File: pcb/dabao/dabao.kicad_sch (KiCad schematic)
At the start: 83 parts, among them J1 USB_C_Receptacle_USB2.0_16P, J2 USB_C_Receptacle_USB2.0_16P, J3 Conn_01x04_Pin, J4 Conn_01x04_Pin, J5 Conn_Battery, J6 MJ-4PP-9, SW1 SW_RESET, SW2 SW_POWER, U1 nice_nano, U2 MCP23017_SP, U3 MCP23017_SO

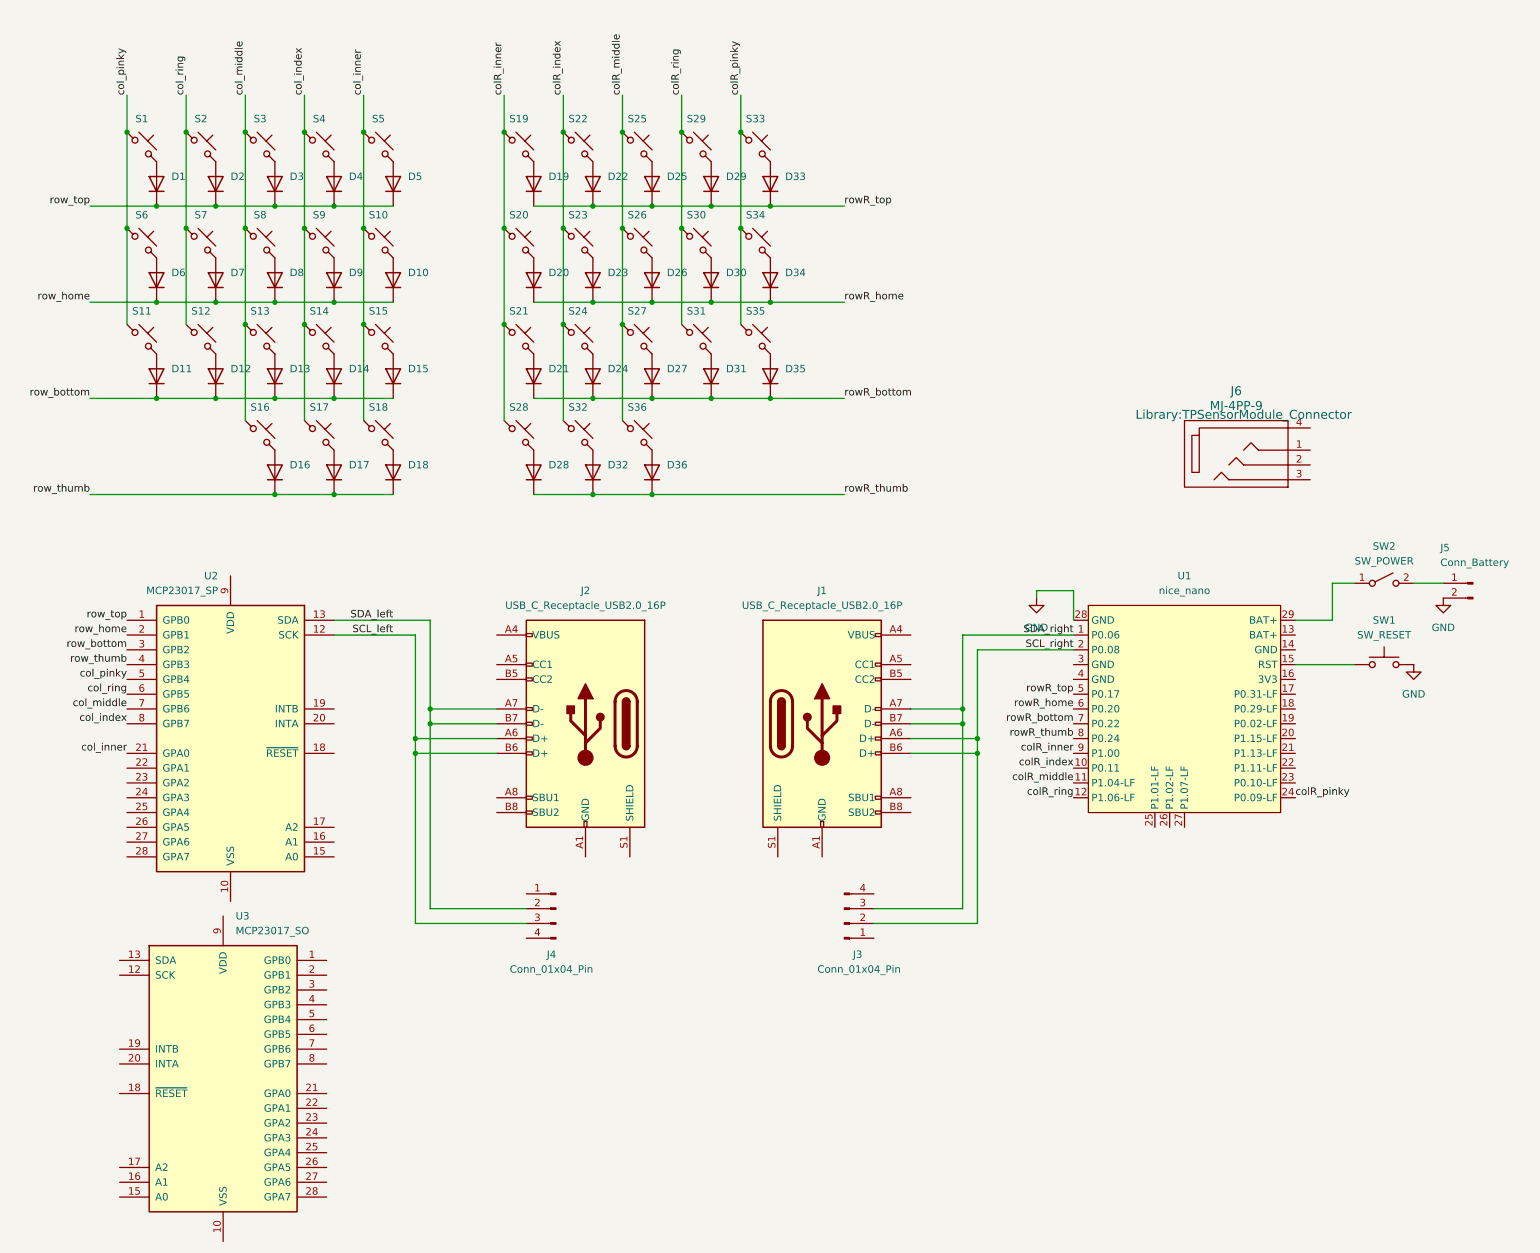
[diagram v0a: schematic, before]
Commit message: Make reversible pcb
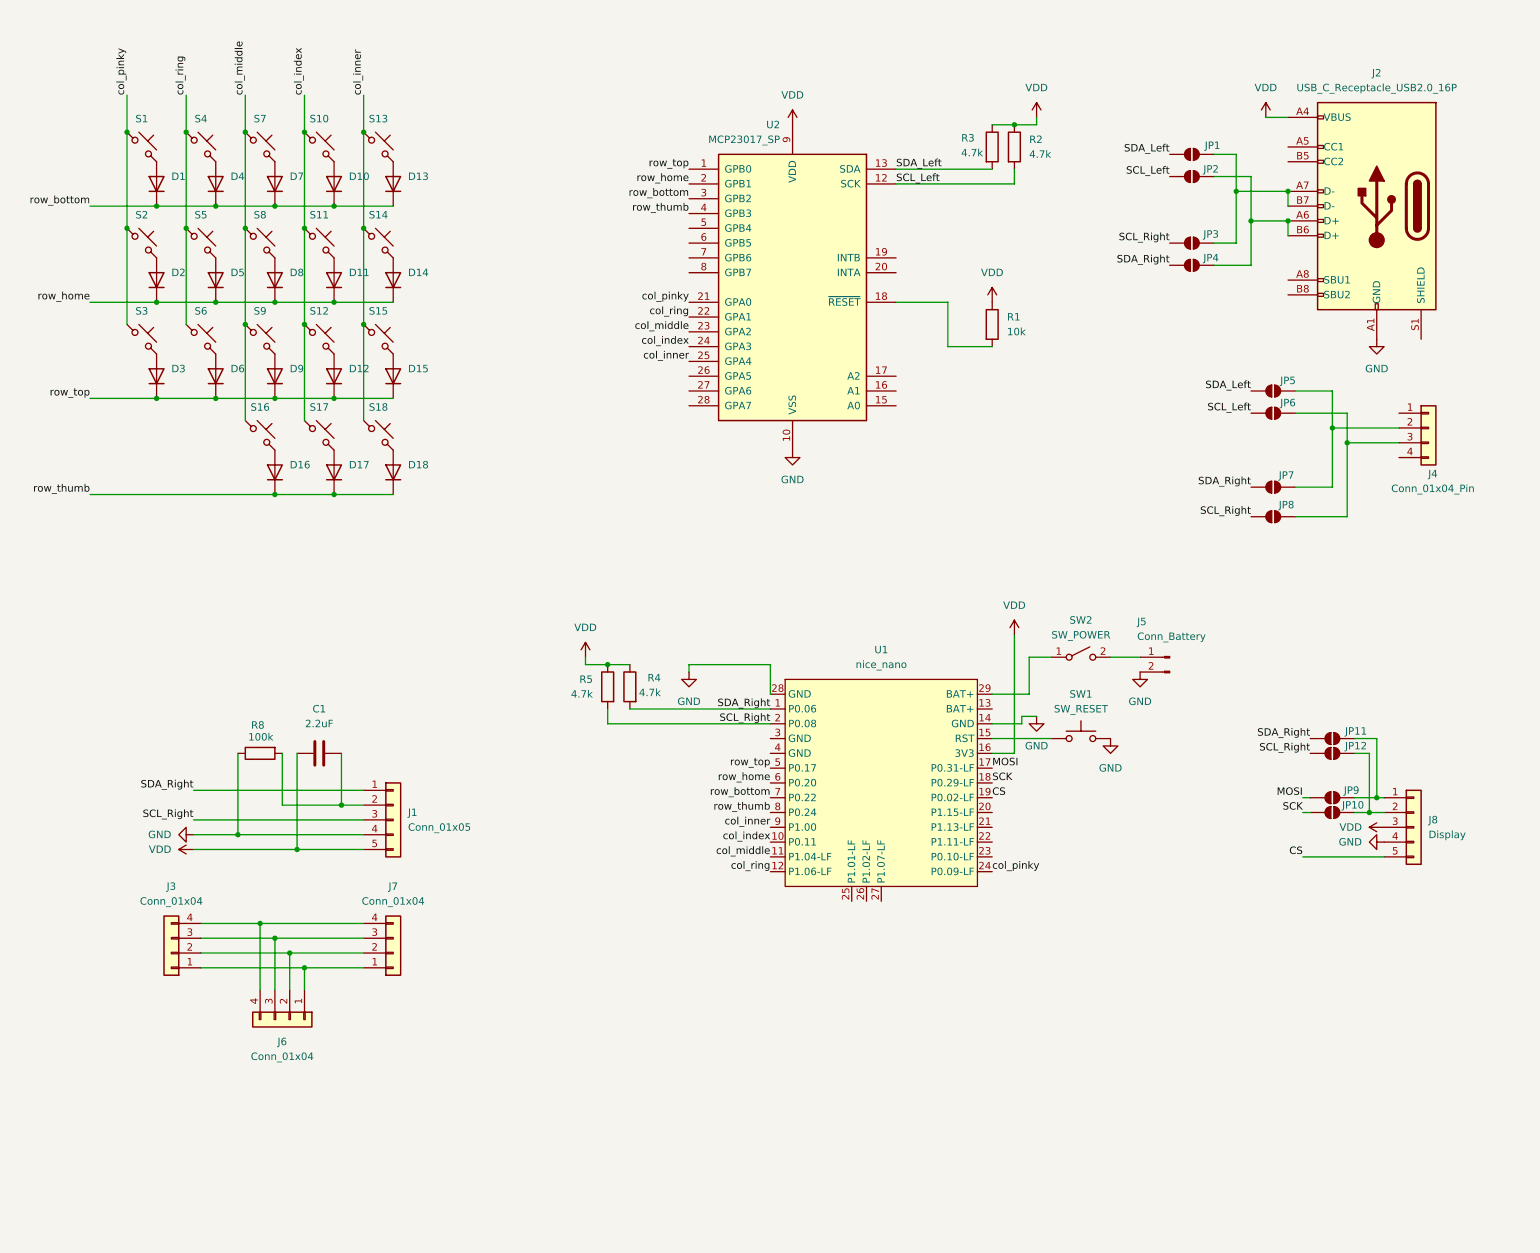
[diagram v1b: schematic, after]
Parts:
- removed D19, D20, D21, D22, D23, D24, D25, D26, D27, D28, D29, D30, D31, D32, D33, D34, D35, D36: 1N4148, Diode_THT:D_DO-35_SOD27_P7.62mm_Horizontal, symbol Diode:1N4148
- removed J1: USB_C_Receptacle_USB2.0_16P, Connector_USB:USB_C_Receptacle_GCT_USB4085, symbol Connector:USB_C_Receptacle_USB2.0_16P
- removed J3: Conn_01x04_Pin, Library:PinMagnetic_1x04_P2.54mm, symbol Connector:Conn_01x04_Pin
- removed J6: MJ-4PP-9, Library:TPSensorModule_Connector, symbol TPS42:MJ-4PP-9
- removed S19, S20, S21, S22, S23, S24, S25, S26, S27, S28, S29, S30, S31, S32, S33, S34, S35, S36: choc_v1_SW_HS, PCM_marbastlib-choc:SW_choc_v1_HS_CPG135001S30_1u, symbol PCM_marbastlib-choc:choc_v1_SW_HS_CPG135001S30
- removed U3: MCP23017_SO, Package_SO:SOIC-28W_7.5x17.9mm_P1.27mm, symbol Interface_Expansion:MCP23017_SO
- added C1: 2.2uF, Capacitor_SMD:C_0805_2012Metric, symbol Device:C
- added J1: Conn_01x05, Library:TPModule, symbol Connector_Generic:Conn_01x05
- added J3, J6, J7: Conn_01x04, Library:TPSensorModule_Connector, symbol Connector_Generic:Conn_01x04
- added J8: Display, Connector_PinHeader_2.54mm:PinHeader_1x05_P2.54mm_Vertical, symbol Connector_Generic:Conn_01x05
- added JP1, JP10, JP11, JP12, JP2, JP3, JP4, JP5, JP6, JP7, JP8, JP9: SolderJumper_2_Open, Jumper:SolderJumper-2_P1.3mm_Open_TrianglePad1.0x1.5mm, symbol Jumper:SolderJumper_2_Open
- added R1: 10k, Resistor_SMD:R_0805_2012Metric, symbol Device:R
- added R2, R3, R4, R5: 4.7k, Resistor_SMD:R_0805_2012Metric, symbol Device:R
- added R8: 100k, Resistor_SMD:R_0805_2012Metric, symbol Device:R
- D1, D15, D16, D17, D18, D8: footprint Diode_THT:D_DO-35_SOD27_P7.62mm_Horizontal -> Library:D_SOD-323_HandSoldering_Reversable
- D10: renamed from D4; footprint Diode_THT:D_DO-35_SOD27_P7.62mm_Horizontal -> Library:D_SOD-323_HandSoldering_Reversable
- D11: renamed from D9; footprint Diode_THT:D_DO-35_SOD27_P7.62mm_Horizontal -> Library:D_SOD-323_HandSoldering_Reversable
- D12: renamed from D14; footprint Diode_THT:D_DO-35_SOD27_P7.62mm_Horizontal -> Library:D_SOD-323_HandSoldering_Reversable
- D13: renamed from D5; footprint Diode_THT:D_DO-35_SOD27_P7.62mm_Horizontal -> Library:D_SOD-323_HandSoldering_Reversable
- D14: renamed from D10; footprint Diode_THT:D_DO-35_SOD27_P7.62mm_Horizontal -> Library:D_SOD-323_HandSoldering_Reversable
- D2: renamed from D6; footprint Diode_THT:D_DO-35_SOD27_P7.62mm_Horizontal -> Library:D_SOD-323_HandSoldering_Reversable
- D3: renamed from D11; footprint Diode_THT:D_DO-35_SOD27_P7.62mm_Horizontal -> Library:D_SOD-323_HandSoldering_Reversable
- D4: renamed from D2; footprint Diode_THT:D_DO-35_SOD27_P7.62mm_Horizontal -> Library:D_SOD-323_HandSoldering_Reversable
- D5: renamed from D7; footprint Diode_THT:D_DO-35_SOD27_P7.62mm_Horizontal -> Library:D_SOD-323_HandSoldering_Reversable
- D6: renamed from D12; footprint Diode_THT:D_DO-35_SOD27_P7.62mm_Horizontal -> Library:D_SOD-323_HandSoldering_Reversable
- D7: renamed from D3; footprint Diode_THT:D_DO-35_SOD27_P7.62mm_Horizontal -> Library:D_SOD-323_HandSoldering_Reversable
- D9: renamed from D13; footprint Diode_THT:D_DO-35_SOD27_P7.62mm_Horizontal -> Library:D_SOD-323_HandSoldering_Reversable
- J4: symbol Connector:Conn_01x04_Pin -> Connector_Generic:Conn_01x04
- S1, S15, S17, S18, S8: footprint PCM_marbastlib-choc:SW_choc_v1_HS_CPG135001S30_1u -> Library:Kailh_socket_PG1350_optional_reversible.kicad_mod
- S10: renamed from S4; footprint PCM_marbastlib-choc:SW_choc_v1_HS_CPG135001S30_1u -> Library:Kailh_socket_PG1350_optional_reversible.kicad_mod
- S11: renamed from S9; footprint PCM_marbastlib-choc:SW_choc_v1_HS_CPG135001S30_1u -> Library:Kailh_socket_PG1350_optional_reversible.kicad_mod
- S12: renamed from S14; footprint PCM_marbastlib-choc:SW_choc_v1_HS_CPG135001S30_1u -> Library:Kailh_socket_PG1350_optional_reversible.kicad_mod
- S13: renamed from S5; footprint PCM_marbastlib-choc:SW_choc_v1_HS_CPG135001S30_1u -> Library:Kailh_socket_PG1350_optional_reversible.kicad_mod
- S14: renamed from S10; footprint PCM_marbastlib-choc:SW_choc_v1_HS_CPG135001S30_1u -> Library:SW_PG1350_reversible
- S16: footprint PCM_marbastlib-choc:SW_choc_v1_HS_CPG135001S30_1u -> Library:SW_PG1350_reversible
- S2: renamed from S6; footprint PCM_marbastlib-choc:SW_choc_v1_HS_CPG135001S30_1u -> Library:Kailh_socket_PG1350_optional_reversible.kicad_mod
- S3: renamed from S11; footprint PCM_marbastlib-choc:SW_choc_v1_HS_CPG135001S30_1u -> Library:Kailh_socket_PG1350_optional_reversible.kicad_mod
- S4: renamed from S2; footprint PCM_marbastlib-choc:SW_choc_v1_HS_CPG135001S30_1u -> Library:Kailh_socket_PG1350_optional_reversible.kicad_mod
- S5: renamed from S7; footprint PCM_marbastlib-choc:SW_choc_v1_HS_CPG135001S30_1u -> Library:Kailh_socket_PG1350_optional_reversible.kicad_mod
- S6: renamed from S12; footprint PCM_marbastlib-choc:SW_choc_v1_HS_CPG135001S30_1u -> Library:Kailh_socket_PG1350_optional_reversible.kicad_mod
- S7: renamed from S3; footprint PCM_marbastlib-choc:SW_choc_v1_HS_CPG135001S30_1u -> Library:Kailh_socket_PG1350_optional_reversible.kicad_mod
- S9: renamed from S13; footprint PCM_marbastlib-choc:SW_choc_v1_HS_CPG135001S30_1u -> Library:Kailh_socket_PG1350_optional_reversible.kicad_mod
- U2: footprint Package_DIP:DIP-28_W7.62mm -> Package_SO:SOIC-28W_7.5x17.9mm_P1.27mm; Footprint-DIP (none) -> Package_DIP:DIP-28_W7.62mm
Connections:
- net colR_index is gone; now on net col_index: U1.10 (P0.11)
- net colR_inner is gone; now on net col_inner: U1.9 (P1.00)
- net colR_middle is gone; now on net col_middle: U1.11 (P1.04-LF)
- net colR_pinky is gone; now on net col_pinky: U1.24 (P0.09-LF)
- net colR_ring is gone; now on net col_ring: U1.12 (P1.06-LF)
- net rowR_bottom is gone; now on net row_bottom: U1.7 (P0.22)
- net rowR_home is gone; now on net row_home: U1.6 (P0.20)
- net rowR_thumb is gone; now on net row_thumb: U1.8 (P0.24)
- net rowR_top is gone; now on net row_top: U1.5 (P0.17)
- net GND: now also J2.A1 (GND), J2.A12 (GND), J2.B1 (GND), J2.B12 (GND), U1.14 (GND), U2.10 (VSS), J1.4 (Pin_4), J8.4 (Pin_4), R8.1
- net col_index: now also U2.24 (GPA3); no longer U2.8 (GPB7)
- net col_inner: now also U2.25 (GPA4); no longer U2.21 (GPA0)
- net col_middle: now also U2.23 (GPA2); no longer U2.7 (GPB6)
- net col_pinky: now also U2.21 (GPA0); no longer U2.5 (GPB4)
- net col_ring: now also U2.22 (GPA1); no longer U2.6 (GPB5)
- net row_bottom: now also D1.1 (K), D10.1 (K), D13.1 (K), D4.1 (K), D7.1 (K); no longer D12.1 (K), D15.1 (K), D3.1 (K), D6.1 (K), D9.1 (K)
- net row_top: now also D12.1 (K), D15.1 (K), D3.1 (K), D6.1 (K), D9.1 (K); no longer D1.1 (K), D10.1 (K), D13.1 (K), D4.1 (K), D7.1 (K)
- net at U2.18 (~{RESET}): now also R1.2
- net VDD: now reaches U2.9 (VDD)
- net VDD: now also J2.A4 (VBUS), J2.A9 (VBUS), J2.B4 (VBUS), J2.B9 (VBUS), U1.16 (3V3), C1.1, J1.5 (Pin_5), J8.3 (Pin_3), R1.1, R2.1, R3.1, R4.1, R5.1
- net MOSI: now reaches U1.17 (P0.31-LF)
- net MOSI: now also JP9.1 (A)
- net SCK: now reaches U1.18 (P0.29-LF)
- net SCK: now also JP10.1 (A)
- net CS: now reaches U1.19 (P0.02-LF)
- net CS: now also J8.5 (Pin_5)
- net SCL_left: no longer names the net of J2.A6 (D+), J2.B6 (D+)
- net SCL_left: now also JP2.2 (B), JP4.2 (B); no longer J4.3 (Pin_3), U2.12 (SCK)
- net SCL_right renamed SCL_Right
- net SCL_Right: now also J1.3 (Pin_3), JP12.1 (A), JP3.1 (A), JP8.1 (A), R5.2
- net SDA_left: no longer names the net of J2.A7 (D-), J2.B7 (D-)
- net SDA_left: now also JP1.2 (B), JP3.2 (B); no longer J4.2 (Pin_2), U2.13 (SDA)
- net SDA_right renamed SDA_Right
- net SDA_Right: now also J1.1 (Pin_1), JP11.1 (A), JP4.1 (A), JP7.1 (A), R4.2
- new net: J8.2 (Pin_2), JP10.2 (B), JP12.2 (B)
- new net: J4.2 (Pin_2), JP5.2 (B), JP7.2 (B)
- new net: J3.1 (Pin_1), J6.1 (Pin_1), J7.1 (Pin_1)
- new net: J3.2 (Pin_2), J6.2 (Pin_2), J7.2 (Pin_2)
- new net: J3.3 (Pin_3), J6.3 (Pin_3), J7.3 (Pin_3)
- new net: J3.4 (Pin_4), J6.4 (Pin_4), J7.4 (Pin_4)
- new net: C1.2, J1.2 (Pin_2), R8.2
- new net: J8.1 (Pin_1), JP11.2 (B), JP9.2 (B)
- new net: J4.3 (Pin_3), JP6.2 (B), JP8.2 (B)
- new net SCL_Left: JP2.1 (A), JP6.1 (A), R2.2, U2.12 (SCK)
- new net SDA_Left: JP1.1 (A), JP5.1 (A), R3.2, U2.13 (SDA)
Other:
- moved on the sheet: J2, J5, SW1, SW2, U1, U2

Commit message: Update layout
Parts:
- removed R4, R5: 4.7k, Resistor_SMD:R_0805_2012Metric, symbol Device:R
- J5: footprint Connector_JST:JST_EH_S2B-EH_1x02_P2.50mm_Horizontal -> Connector_JST:JST_PH_S2B-PH-K_1x02_P2.00mm_Horizontal; symbol Connector:Conn_01x02_Pin -> Connector_Generic:Conn_01x02
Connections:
- net CS: now also U1.10 (P0.11); no longer U1.19 (P0.02-LF)
- net GND: now also J4.4 (Pin_4), J5.1 (Pin_1); no longer J5.2 (Pin_2)
- net MOSI: now also U1.9 (P1.00); no longer U1.17 (P0.31-LF)
- net SCK: now also U1.7 (P0.22); no longer U1.18 (P0.29-LF)
- net SCL_Right: now also U1.6 (P0.20); no longer J1.3 (Pin_3), U1.2 (P0.08)
- net SDA_Right: now also U1.5 (P0.17); no longer J1.1 (Pin_1), U1.1 (P0.06)
- net VDD: now also J4.1 (Pin_1)
- net col_index: now also U1.21 (P1.13-LF); no longer U1.10 (P0.11)
- net col_inner: now also U1.20 (P1.15-LF); no longer U1.9 (P1.00)
- net col_middle: now also U1.22 (P1.11-LF); no longer U1.11 (P1.04-LF)
- net col_ring: now also U1.23 (P0.10-LF); no longer U1.12 (P1.06-LF)
- net row_bottom: now also U1.19 (P0.02-LF); no longer U1.7 (P0.22)
- net row_home: now also U1.18 (P0.29-LF); no longer U1.6 (P0.20)
- net row_thumb: now also U1.12 (P1.06-LF); no longer U1.8 (P0.24)
- net row_top: now also U1.17 (P0.31-LF); no longer U1.5 (P0.17)
- net at SW2.2 (B): now also J5.2 (Pin_2); no longer J5.1 (Pin_1)
- new net PS2_CLK: J1.3 (Pin_3), U1.2 (P0.08)
- new net PS2_Data: J1.1 (Pin_1), U1.1 (P0.06)
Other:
- moved on the sheet: R1
